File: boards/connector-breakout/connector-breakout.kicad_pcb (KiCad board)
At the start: 2 copper layers, 40 x 75.5 mm, 6 parts, among them J1 Harwin M55-7001242R, J2 Conn_01x12, J3 Conn_01x20, J4 Conn_01x20

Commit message: Schematic and footprints done for rev of solar sim connector board
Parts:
- removed REF** (x2): Hole-2.4mm-NPTH, oresat-misc:Hole-2.4mm-NPTH
- added J6: M55-7101242R, oresat-connectors:J-Harwin-M55-7101242R, F.Cu at (110.5, 67.0)
- J1: value Harwin M55-7001242R -> M55-7001242R; footprint oresat-connectors:J-Harwin-M55-7001242R -> oresat-connectors:J-Harwin-M55-7XX1242R
- J2: value Conn_01x12 -> PRPC012SFAN-RC
- J3, J4: value Conn_01x20 -> 302-S201
- moved J2 48.6 mm to (110.5, 104.8)
- moved J3 48.6 mm to (97.3, 79.4)
- moved J4 48.6 mm to (121.1, 79.4)
- moved J1 48.6 mm to (110.5, 141.4), turned to 0 degrees
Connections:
- J1 pad 7: /AUX -> /SM-UART-TX
- J1 pad 8: /AUX -> /SM-UART-RX
- J2 pad 7: /AUX -> /SM-UART-TX
- J2 pad 8: /AUX -> /SM-UART-RX
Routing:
- net /AUX: track 61.4 -> 0.00 mm
- net (no net): track 0.00 -> 7.17 mm

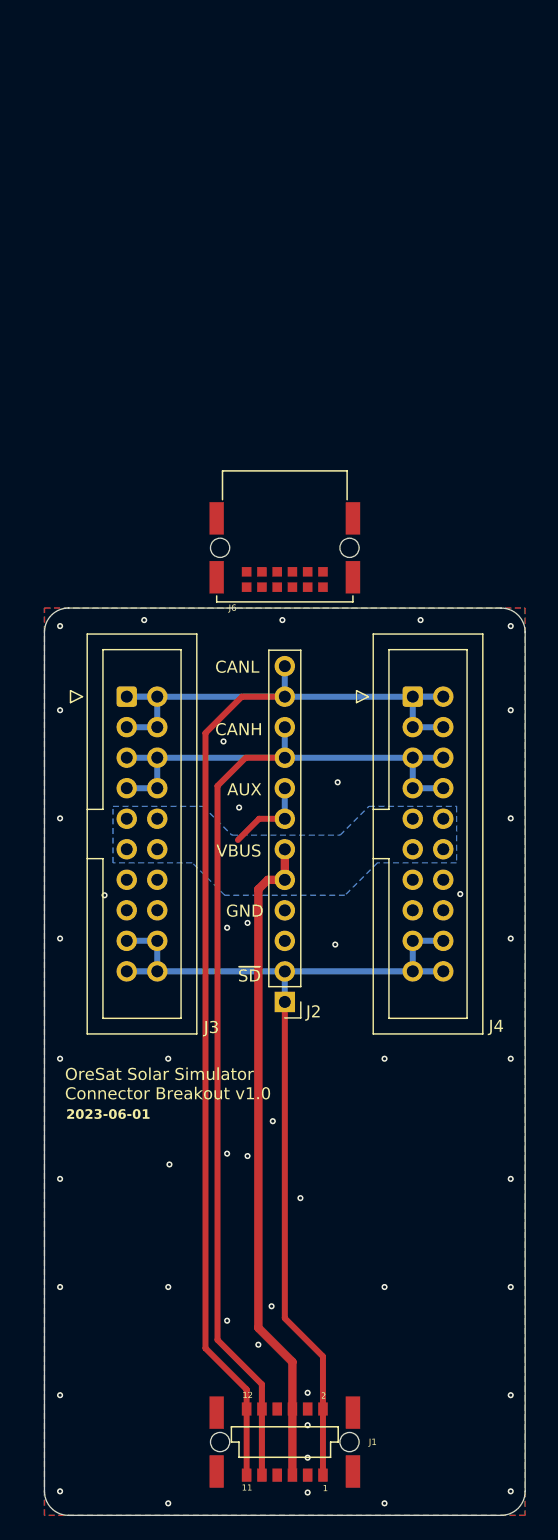
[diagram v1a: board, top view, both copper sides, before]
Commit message: Update with connector moved
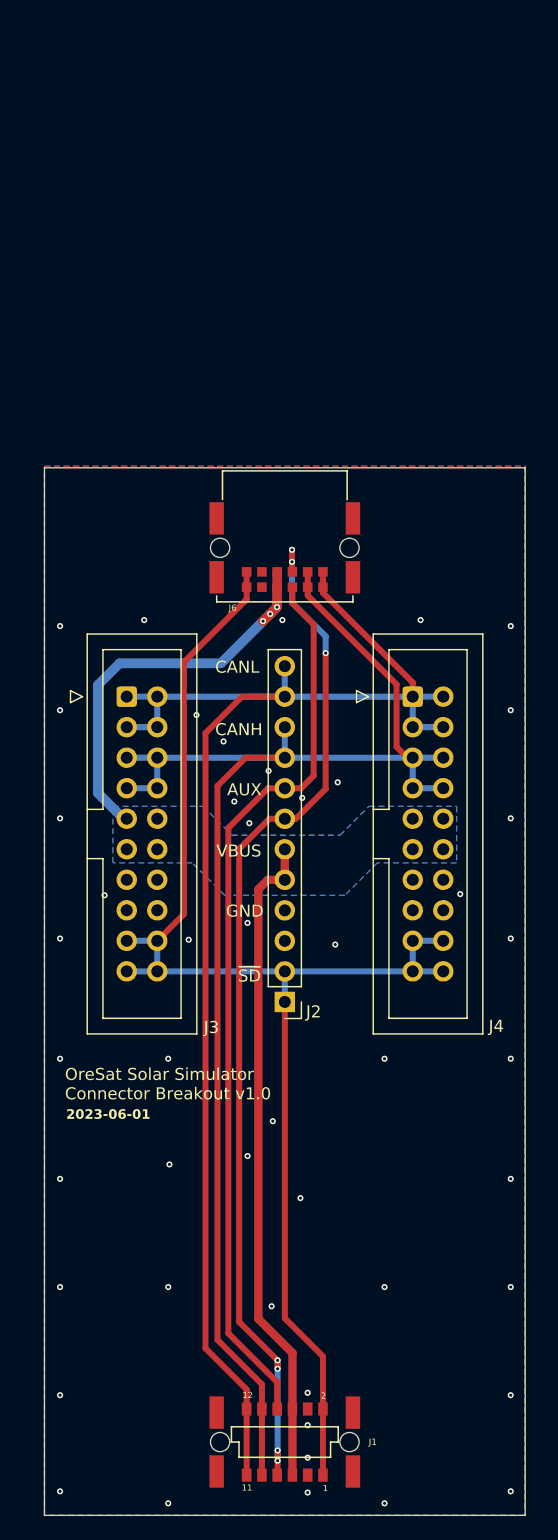
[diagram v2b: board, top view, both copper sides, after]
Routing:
- net /SM-UART-TX: track 0.00 -> 87.2 mm, vias 0 -> 7
- net /SM-UART-RX: track 0.00 -> 75.4 mm
- net VBUS: track 55.0 -> 89.4 mm, vias 0 -> 3
- net /~{SD}: track 79.7 -> 113.5 mm
- net /CANH: track 104.5 -> 123.8 mm
- net /CANL: track 110.1 -> 124.8 mm
- net (no net): track 7.17 -> 0.00 mm
- net GND: vias 47 -> 48
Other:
- board size 40 x 75.5 mm -> 40 x 87.2 mm

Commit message: Layout updated with connector changes
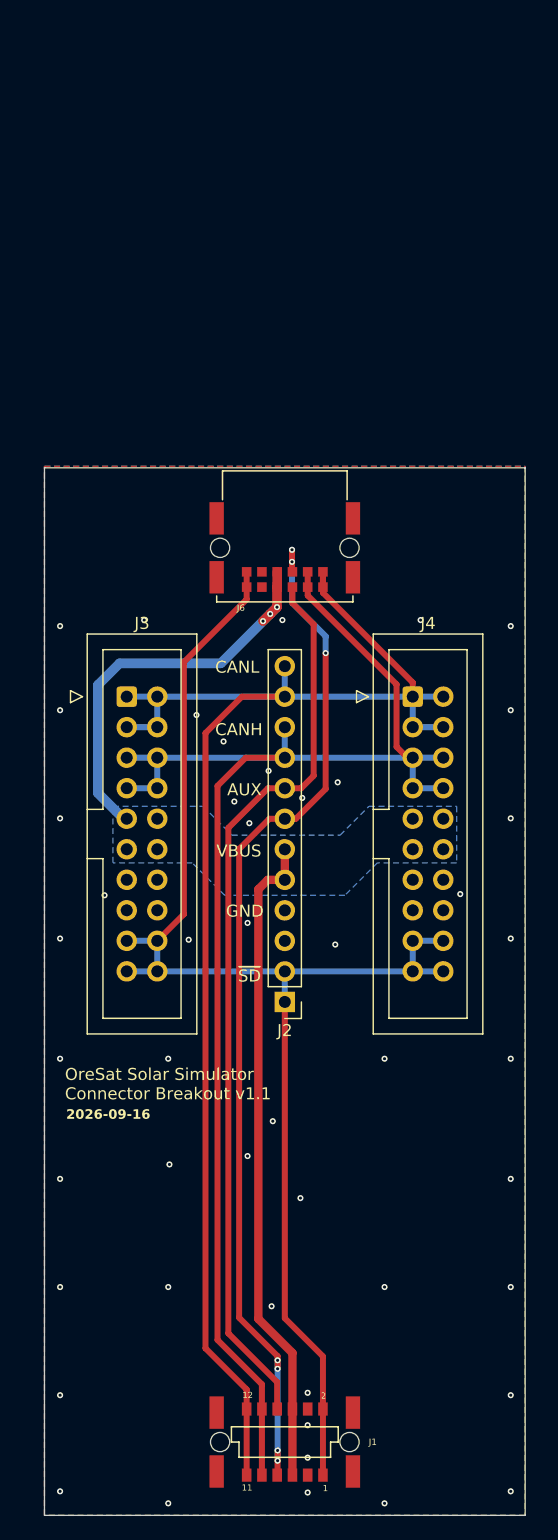
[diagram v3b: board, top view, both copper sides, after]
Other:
- board text added: "2026-09-16"
- board text added: "OreSat Solar Simulator Connector Breakout v1.1"
- board text removed: "2023-06-01"
- board text removed: "OreSat Solar Simulator Connector Breakout v1.0"

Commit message: Solar Simulator Connector Board v1.1
Recovered missing holes, added fiducials, brought up to modern standards with stackup, makefile, and readme, fixed stiching and date, checked BOM, should be good to go.
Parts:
- added FID1: Fiducial, Fiducial:Fiducial_1mm_Mask2mm, F.Cu at (94.0, 65.0)
- added FID2: Fiducial, Fiducial:Fiducial_1mm_Mask2mm, F.Cu at (126.0, 65.0)
- added FID3: Fiducial, Fiducial:Fiducial_1mm_Mask2mm, F.Cu at (94.0, 144.0)
- added H1: MountingHole, MountingHole:MountingHole_2.2mm_M2_ISO14580, F.Cu at (99.0, 141.6)
- added H2: MountingHole, MountingHole:MountingHole_2.2mm_M2_ISO14580, F.Cu at (122.0, 141.6)
- J1: value M55-7001242R -> Conn_01x12_MountingPin
- J6: value M55-7101242R -> Conn_01x12_MountingPin
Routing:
- net GND: vias 48 -> 59
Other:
- rule pad_to_mask_clearance: 0.0508 -> 0
- rule solder_mask_min_width: 0.101 -> 0.1016
- board text added: "${TITLE} v${REVISION} ${ISSUE_DATE}"
- board text removed: "2026-09-16"
- board text removed: "OreSat Solar Simulator Connector Breakout v1.1"
